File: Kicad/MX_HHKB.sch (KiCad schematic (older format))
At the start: 142 parts, among them J1 USB_mini_micro_B, K1 Esc, K10 9, K11 0, K12 -, K13 =, K14 Tab, K15 Q, K16 W, K17 E, K18 R, K19 T, K2 1, K20 Y, K21 U, K22 I, K23 O, K24 P, K25 [, K26 ], K27 Ctrl, K28 A, K29 S, K3 2, K30 D, K31 F, K32 G, K33 H, K34 J, K35 K, K36 L, K37 ;, K38 ', K39 Enter, K4 3, K40 L_Shift, K41 Z, K42 X, K43 C, K44 V, K45 B, K46 N, K47 M, K48 ,, K49 ., K5 4, K50 /, K51 R_Shift, K52 Fn, K53 L_GUI, K54 L_ALT, K55 SPACE, K56 R_ALT, K57 R_GUI, K58 `, K59 \\, K6 5, K60 BACKSPACE, K61 Ctrl, K7 6, K8 7, K9 8, SW1 SW_PUSH, U0 ATMEGA32U4, X1 XTAL_GND

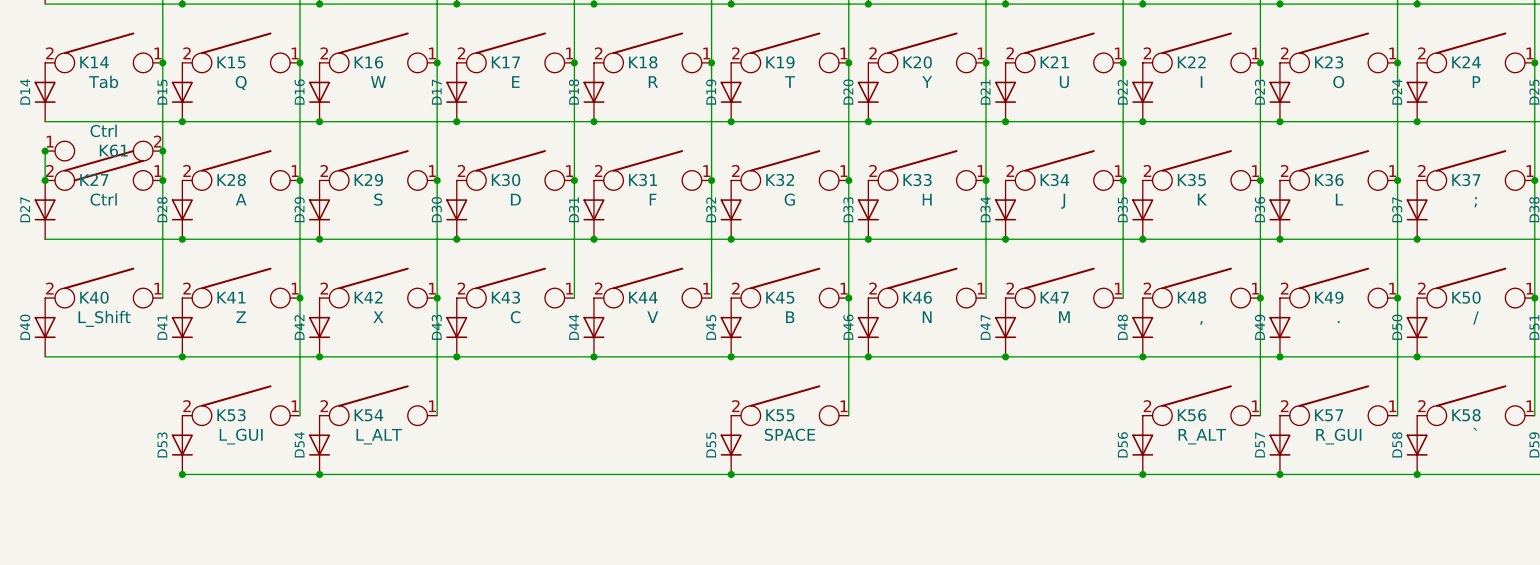
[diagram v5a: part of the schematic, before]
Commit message: - Updated layout to allow choice in 3 combinations for bottom row
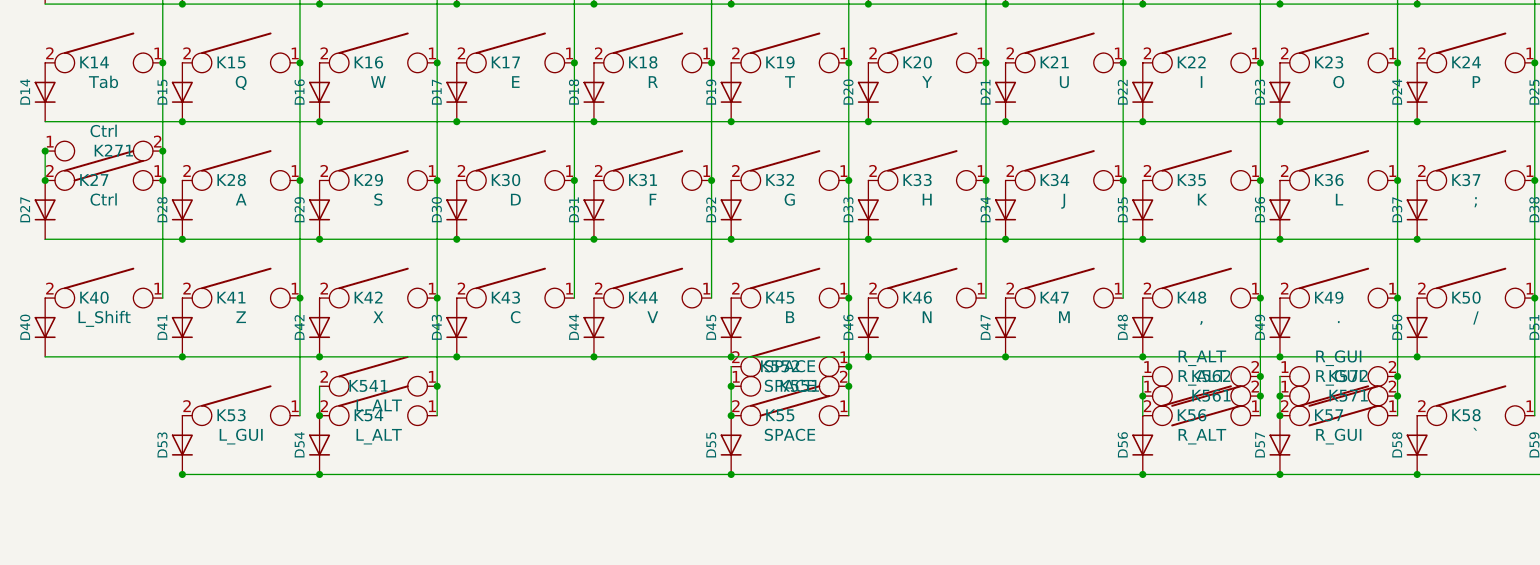
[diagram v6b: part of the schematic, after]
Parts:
- added K541: L_ALT, Footprint:Mx_Alps_125, symbol KEYSW
- added K551: SPACE, Footprint:Mx_Alps_600, symbol KEYSW
- added K552: SPACE, Footprint:Mx_Alps_700, symbol KEYSW
- added K561: R_ALT, Footprint:Mx_Alps_150, symbol KEYSW
- added K562: R_ALT, Footprint:Mx_Alps_125, symbol KEYSW
- added K571, K572: R_GUI, Footprint:Mx_Alps_100, symbol KEYSW
- renumbered K61 to K271
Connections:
- net Col2: now also K541.1
- net Col5: now also K551.2, K552.1
- net Col8: now also K561.2, K562.2
- net Col9: now also K571.2, K572.2
- net at D56.2 (A), K56.2: now also K561.1, K562.1
- net at D54.2 (A), K54.2: now also K541.2
- net at D55.2 (A), K55.2: now also K551.1, K552.2
- net at D57.2 (A), K57.2: now also K571.1, K572.1
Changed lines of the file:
@@
 	3000 6550 2000 6550
 $Comp
-L KEYSW K61
+L KEYSW K271
 U 1 1 59062EBC
 P 1050 2150
-F 0 "K61" H 1000 2150 60  0000 C CNN
+F 0 "K271" H 1000 2150 60  0000 C CNN
 F 1 "Ctrl" H 1050 2050 60  0000 C CNN
 F 2 "Footprint:Mx_Alps_175_STEPPED" H 1050 2150 60  0001 C CNN
@@
 	9700 4700 9700 5000
 Connection ~ 9700 5000
+$Comp
+L KEYSW K551
+U 1 1 590B831B
+P 4550 3350
+F 0 "K551" H 4500 3350 60  0000 C CNN
+F 1 "SPACE" H 4550 3250 60  0000 C CNN
+F 2 "Footprint:Mx_Alps_600" H 4550 3350 60  0001 C CNN
+F 3 "" H 4550 3350 60  0000 C CNN
+	1    4550 3350
+	-1   0    0    1
+$EndComp
+Connection ~ 4850 3350
+Wire Wire Line
+	4250 3250 4250 3500
+Connection ~ 4250 3500
+$Comp
+L KEYSW K541
+U 1 1 590B8C51
+P 2450 3350
+F 0 "K541" H 2400 3350 60  0000 C CNN
+F 1 "L_ALT" H 2450 3250 60  0000 C CNN
+F 2 "Footprint:Mx_Alps_125" H 2450 3350 60  0001 C CNN
+F 3 "" H 2450 3350 60  0000 C CNN
+	1    2450 3350
+	1    0    0    -1
+$EndComp
+Wire Wire Line
+	2150 3350 2150 3500
+Connection ~ 2150 3500
+Connection ~ 2750 3350
+$Comp
+L KEYSW K552
+U 1 1 590D1F5C
+P 4550 3250
+F 0 "K552" H 4500 3250 60  0000 C CNN
+F 1 "SPACE" H 4550 3150 60  0000 C CNN
+F 2 "Footprint:Mx_Alps_700" H 4550 3250 60  0001 C CNN
+F 3 "" H 4550 3250 60  0000 C CNN
+	1    4550 3250
+	1    0    0    -1
+$EndComp
+Connection ~ 4250 3350
+Connection ~ 4850 3250
+$Comp
+L KEYSW K561
+U 1 1 590D368C
+P 6650 3400
+F 0 "K561" H 6600 3400 60  0000 C CNN
+F 1 "R_ALT" H 6650 3300 60  0000 C CNN
+F 2 "Footprint:Mx_Alps_150" H 6650 3400 60  0001 C CNN
+F 3 "" H 6650 3400 60  0000 C CNN
+	1    6650 3400
+	-1   0    0    1
+$EndComp
+Wire Wire Line
+	6350 3300 6350 3500
+Connection ~ 6950 3400
+$Comp
+L KEYSW K562
+U 1 1 590D4921
+P 6650 3300
+F 0 "K562" H 6600 3300 60  0000 C CNN
+F 1 "R_ALT" H 6650 3200 60  0000 C CNN
+F 2 "Footprint:Mx_Alps_125" H 6650 3300 60  0001 C CNN
+F 3 "" H 6650 3300 60  0000 C CNN
+	1    6650 3300
+	-1   0    0    1
+$EndComp
+Connection ~ 6350 3400
+Connection ~ 6950 3300
+$Comp
+L KEYSW K571
+U 1 1 590D5BF1
+P 7350 3400
+F 0 "K571" H 7300 3400 60  0000 C CNN
+F 1 "R_GUI" H 7350 3300 60  0000 C CNN
+F 2 "Footprint:Mx_Alps_100" H 7350 3400 60  0001 C CNN
+F 3 "" H 7350 3400 60  0000 C CNN
+	1    7350 3400
+	-1   0    0    1
+$EndComp
+Wire Wire Line
+	7050 3300 7050 3500
+Connection ~ 7050 3500
+Connection ~ 7650 3400
+$Comp
+L KEYSW K572
+U 1 1 590D67BA
+P 7350 3300
+F 0 "K572" H 7300 3300 60  0000 C CNN
+F 1 "R_GUI" H 7350 3200 60  0000 C CNN
+F 2 "Footprint:Mx_Alps_100" H 7350 3300 60  0001 C CNN
+F 3 "" H 7350 3300 60  0000 C CNN
+	1    7350 3300
+	-1   0    0    1
+$EndComp
+Connection ~ 7650 3300
+Connection ~ 7050 3400
 $EndSCHEMATC

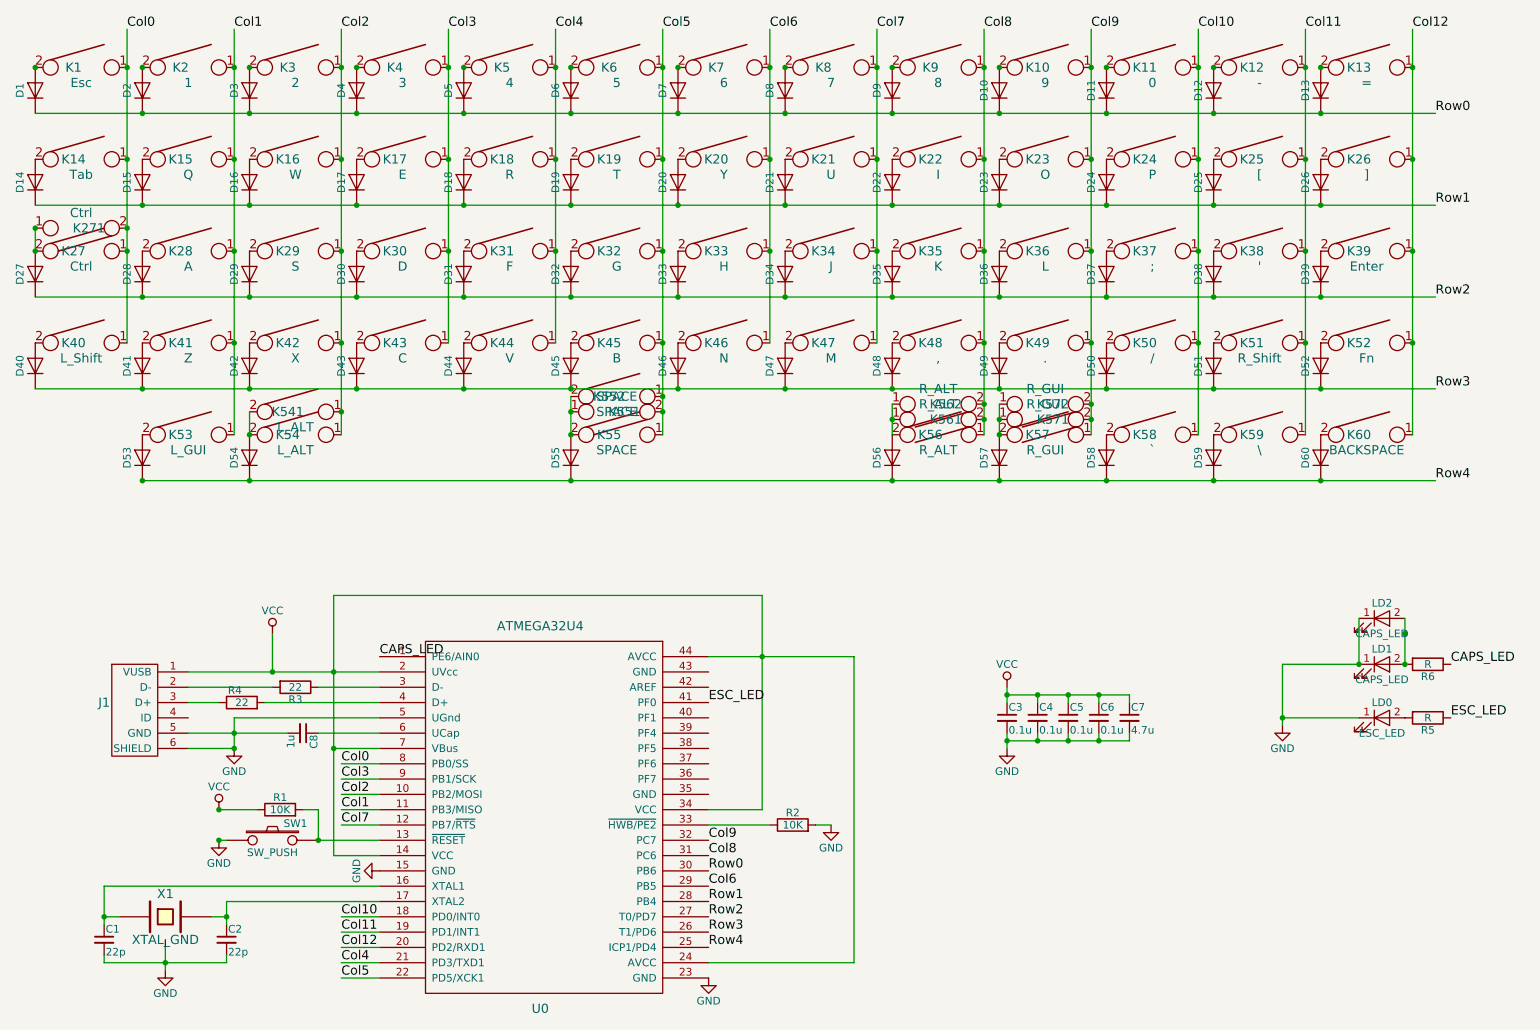
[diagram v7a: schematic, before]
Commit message: - Updated switches label (K00 to K4C) - Fixed footprint - Updated gerber files
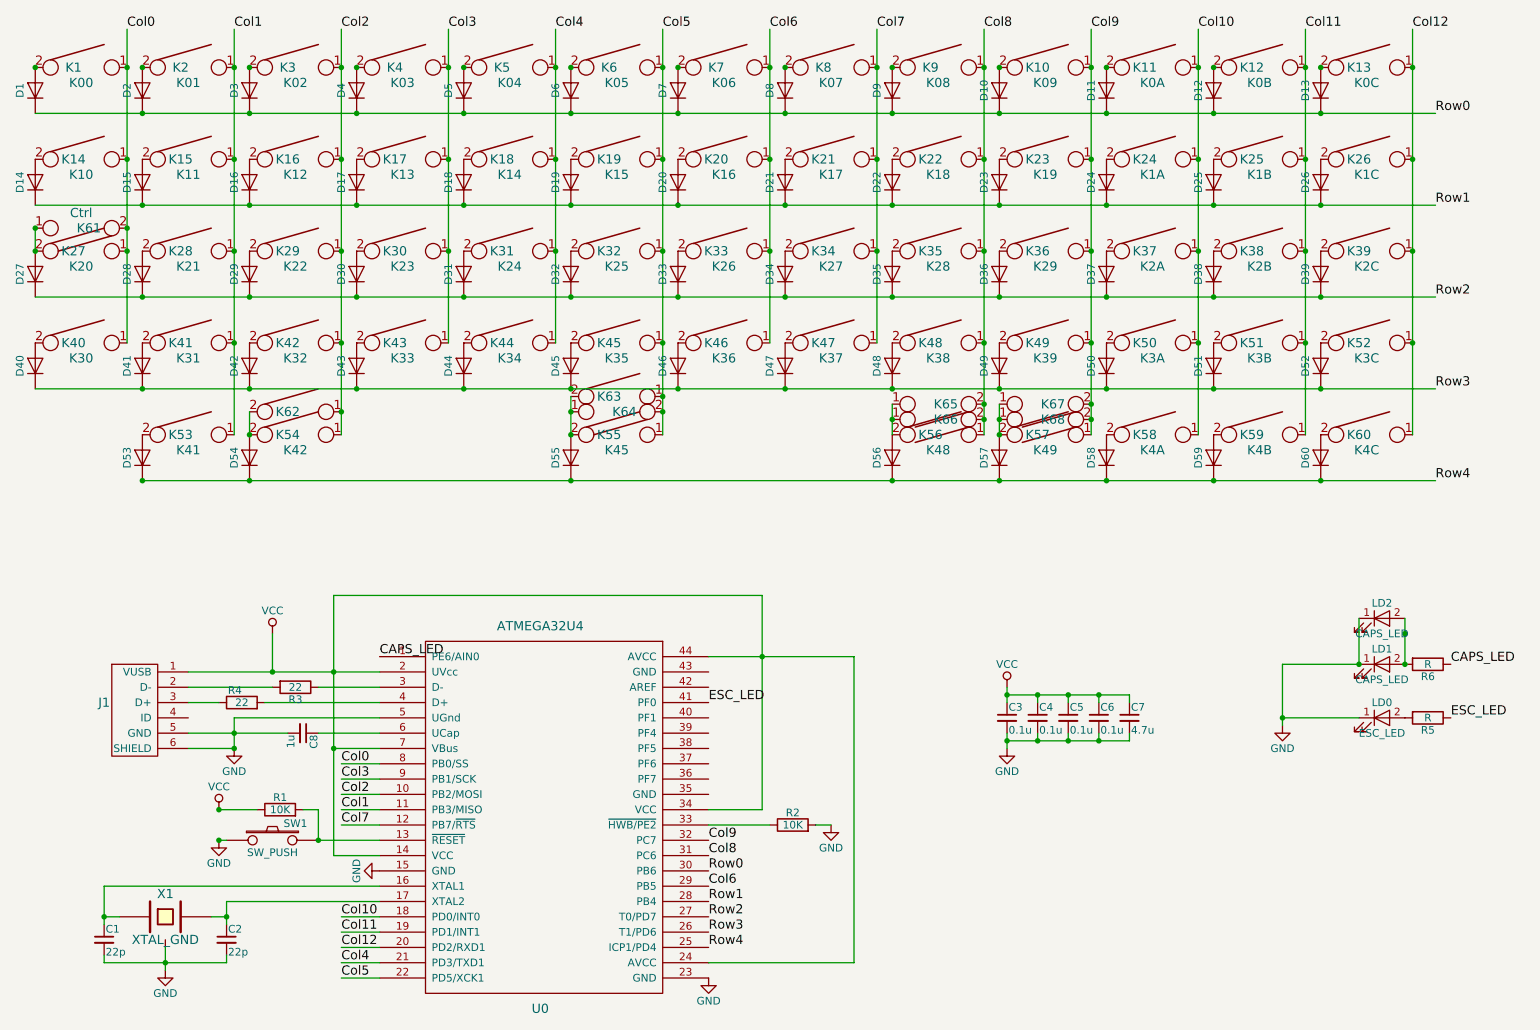
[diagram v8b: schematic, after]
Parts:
- D1, D10, D11, D12, D13, D14, D15, D16, D17, D18, D19, D2, D20, D21, D22, D23, D24, D25, D26, D27, D28, D29, D3, D30, D31, D32, D33, D34, D35, D36, D37, D38, D39, D4, D40, D41, D42, D43, D44, D45, D46, D47, D48, D49, D5, D50, D51, D52, D53, D54, D55, D56, D57, D58, D59, D6, D60, D7, D8, D9: footprint Fooprints:D_SOD123_axial -> Footprint:D_SOD123_axial
- J1: footprint Fooprints:USB_miniB_hirose_5S8 -> Footprint:USB_miniB_hirose_5S8
- K1: value Esc -> K00; footprint Fooprints:Mx_Alps_100 -> Footprint:Mx_Alps_100
- K10: value 9 -> K09; footprint Fooprints:Mx_Alps_100 -> Footprint:Mx_Alps_100
- K11: value 0 -> K0A; footprint Fooprints:Mx_Alps_100 -> Footprint:Mx_Alps_100
- K12: value - -> K0B; footprint Fooprints:Mx_Alps_100 -> Footprint:Mx_Alps_100
- K13: value = -> K0C; footprint Fooprints:Mx_Alps_100 -> Footprint:Mx_Alps_100
- K14: value Tab -> K10; footprint Fooprints:Mx_Alps_150 -> Footprint:Mx_Alps_150
- K15: value Q -> K11; footprint Fooprints:Mx_Alps_100 -> Footprint:Mx_Alps_100
- K16: value W -> K12; footprint Fooprints:Mx_Alps_100 -> Footprint:Mx_Alps_100
- K17: value E -> K13; footprint Fooprints:Mx_Alps_100 -> Footprint:Mx_Alps_100
- K18: value R -> K14; footprint Fooprints:Mx_Alps_100 -> Footprint:Mx_Alps_100
- K19: value T -> K15; footprint Fooprints:Mx_Alps_100 -> Footprint:Mx_Alps_100
- K2: value 1 -> K01; footprint Fooprints:Mx_Alps_100 -> Footprint:Mx_Alps_100
- K20: value Y -> K16; footprint Fooprints:Mx_Alps_100 -> Footprint:Mx_Alps_100
- K21: value U -> K17; footprint Fooprints:Mx_Alps_100 -> Footprint:Mx_Alps_100
- K22: value I -> K18; footprint Fooprints:Mx_Alps_100 -> Footprint:Mx_Alps_100
- K23: value O -> K19; footprint Fooprints:Mx_Alps_100 -> Footprint:Mx_Alps_100
- K24: value P -> K1A; footprint Fooprints:Mx_Alps_100 -> Footprint:Mx_Alps_100
- K25: value [ -> K1B; footprint Fooprints:Mx_Alps_100 -> Footprint:Mx_Alps_100
- K26: value ] -> K1C; footprint Fooprints:Mx_Alps_100 -> Footprint:Mx_Alps_100
- K27: value Ctrl -> K20; footprint Fooprints:Mx_Alps_175 -> Footprint:Mx_Alps_175
- K28: value A -> K21; footprint Fooprints:Mx_Alps_100 -> Footprint:Mx_Alps_100
- K29: value S -> K22; footprint Fooprints:Mx_Alps_100 -> Footprint:Mx_Alps_100
- K3: value 2 -> K02; footprint Fooprints:Mx_Alps_100 -> Footprint:Mx_Alps_100
- K30: value D -> K23; footprint Fooprints:Mx_Alps_100 -> Footprint:Mx_Alps_100
- K31: value F -> K24; footprint Fooprints:Mx_Alps_100 -> Footprint:Mx_Alps_100
- K32: value G -> K25; footprint Fooprints:Mx_Alps_100 -> Footprint:Mx_Alps_100
- K33: value H -> K26; footprint Fooprints:Mx_Alps_100 -> Footprint:Mx_Alps_100
- K34: value J -> K27; footprint Fooprints:Mx_Alps_100 -> Footprint:Mx_Alps_100
- K35: value K -> K28; footprint Fooprints:Mx_Alps_100 -> Footprint:Mx_Alps_100
- K36: value L -> K29; footprint Fooprints:Mx_Alps_100 -> Footprint:Mx_Alps_100
- K37: value ; -> K2A; footprint Fooprints:Mx_Alps_100 -> Footprint:Mx_Alps_100
- K38: value ' -> K2B; footprint Fooprints:Mx_Alps_100 -> Footprint:Mx_Alps_100
- K39: value Enter -> K2C; footprint Fooprints:Mx_Alps_225 -> Footprint:Mx_Alps_225
- K4: value 3 -> K03; footprint Fooprints:Mx_Alps_100 -> Footprint:Mx_Alps_100
- K40: value L_Shift -> K30; footprint Fooprints:Mx_Alps_175 -> Footprint:Mx_Alps_175
- K41: value Z -> K31; footprint Fooprints:Mx_Alps_100 -> Footprint:Mx_Alps_100
- K42: value X -> K32; footprint Fooprints:Mx_Alps_100 -> Footprint:Mx_Alps_100
- K43: value C -> K33; footprint Fooprints:Mx_Alps_100 -> Footprint:Mx_Alps_100
- K44: value V -> K34; footprint Fooprints:Mx_Alps_100 -> Footprint:Mx_Alps_100
- K45: value B -> K35; footprint Fooprints:Mx_Alps_100 -> Footprint:Mx_Alps_100
- K46: value N -> K36; footprint Fooprints:Mx_Alps_100 -> Footprint:Mx_Alps_100
- K47: value M -> K37; footprint Fooprints:Mx_Alps_100 -> Footprint:Mx_Alps_100
- K48: value , -> K38; footprint Fooprints:Mx_Alps_100 -> Footprint:Mx_Alps_100
- K49: value . -> K39; footprint Fooprints:Mx_Alps_100 -> Footprint:Mx_Alps_100
- K5: value 4 -> K04; footprint Fooprints:Mx_Alps_100 -> Footprint:Mx_Alps_100
- K50: value / -> K3A; footprint Fooprints:Mx_Alps_100 -> Footprint:Mx_Alps_100
- K51: value R_Shift -> K3B; footprint Fooprints:Mx_Alps_125 -> Footprint:Mx_Alps_125
- K52: value Fn -> K3C; footprint Fooprints:Mx_Alps_100 -> Footprint:Mx_Alps_100
- K53: value L_GUI -> K41; footprint Fooprints:Mx_Alps_100 -> Footprint:Mx_Alps_100
- K54: value L_ALT -> K42; footprint Fooprints:Mx_Alps_150 -> Footprint:Mx_Alps_150
- K55: value SPACE -> K45; footprint Fooprints:Mx_Alps_625 -> Footprint:Mx_Alps_625
- K56: value R_ALT -> K48; footprint Fooprints:Mx_Alps_150 -> Footprint:Mx_Alps_150
- K57: value R_GUI -> K49; footprint Fooprints:Mx_Alps_100 -> Footprint:Mx_Alps_100
- K58: value ` -> K4A; footprint Fooprints:Mx_Alps_100 -> Footprint:Mx_Alps_100
- K59: value \\ -> K4B; footprint Fooprints:Mx_Alps_100 -> Footprint:Mx_Alps_100
- K6: value 5 -> K05; footprint Fooprints:Mx_Alps_100 -> Footprint:Mx_Alps_100
- K60: value BACKSPACE -> K4C; footprint Fooprints:Mx_Alps_150 -> Footprint:Mx_Alps_150
- K7: value 6 -> K06; footprint Fooprints:Mx_Alps_100 -> Footprint:Mx_Alps_100
- K8: value 7 -> K07; footprint Fooprints:Mx_Alps_100 -> Footprint:Mx_Alps_100
- K9: value 8 -> K08; footprint Fooprints:Mx_Alps_100 -> Footprint:Mx_Alps_100
- renumbered K271 to K61, K541 to K62, K552 to K63, K551 to K64, K562 to K65, K561 to K66, K572 to K67, K571 to K68
